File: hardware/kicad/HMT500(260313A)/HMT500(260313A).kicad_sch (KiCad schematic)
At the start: 0 parts

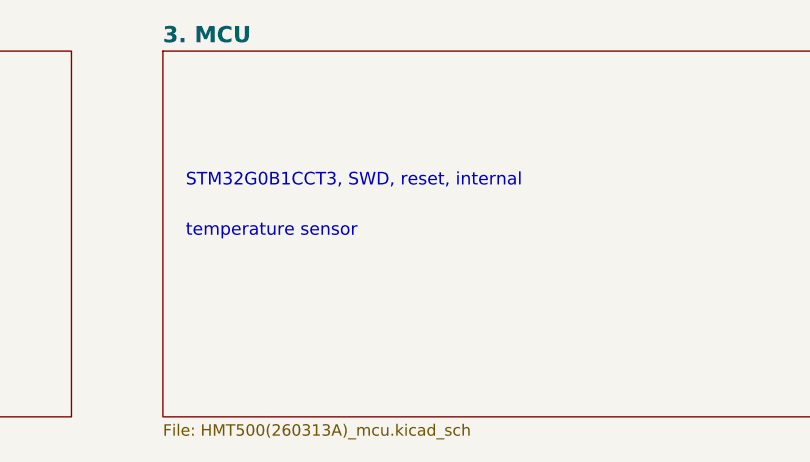
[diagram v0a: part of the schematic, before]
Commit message: Decision #39: sample stage uses JLCPCB parts - MCU STM32G0B1CCT6
Same die and pinout as CCT3 (85 C grade); revisit for production once the
electronics temperature spec is set. 58 of 60 BOM lines have LCSC numbers.

Co-Authored-By: Claude Opus 5.5 <noreply@anthropic.com>
Claude-Session: https://claude.ai/code/session_01JA2o8uJsqp9Vzsg4b665ev
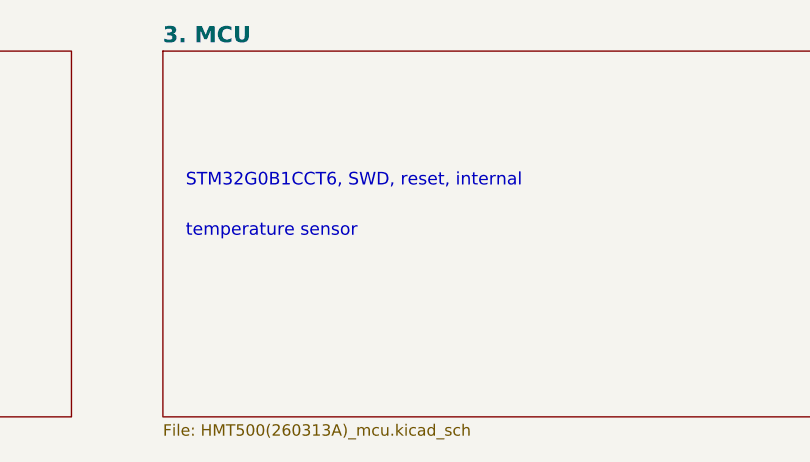
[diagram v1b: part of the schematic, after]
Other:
- note added: "STM32G0B1CCT6, SWD, reset, internal"
- note removed: "STM32G0B1CCT3, SWD, reset, internal"
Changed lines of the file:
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@@
 (text "LDO 3.3V" (at 119.38 56.388 0) (effects (font (size 1.4 1.4)) (justify left bottom)))
 (sheet (at 213.36 35.56) (size 86.36 40.64) (fields_autoplaced) (stroke (width 0.1524) (type solid)) (fill (color 0 0 0 0.0000)) (property "Sheetname" "3. MCU" (at 213.36 34.798 0) (effects (font (size 1.8 1.8) bold) (justify left bottom))) (property "Sheetfile" "HMT500(260313A)_mcu.kicad_sch" (at 213.36 76.962 0) (effects (font (size 1.27 1.27)) (justify left top))) (instances (project "HMT500(260313A)" (path "/1ebb025b-11bd-5f7c-aaab-41e2a750e8b3" (page "4")))))
-(text "STM32G0B1CCT3, SWD, reset, internal" (at 215.9 50.8 0) (effects (font (size 1.4 1.4)) (justify left bottom)))
+(text "STM32G0B1CCT6, SWD, reset, internal" (at 215.9 50.8 0) (effects (font (size 1.4 1.4)) (justify left bottom)))
 (text "temperature sensor" (at 215.9 56.388 0) (effects (font (size 1.4 1.4)) (justify left bottom)))
 (sheet (at 309.88 35.56) (size 86.36 40.64) (fields_autoplaced) (stroke (width 0.1524) (type solid)) (fill (color 0 0 0 0.0000)) (property "Sheetname" "4. Measurement" (at 309.88 34.798 0) (effects (font (size 1.8 1.8) bold) (justify left bottom))) (property "Sheetfile" "HMT500(260313A)_measurement.kicad_sch" (at 309.88 76.962 0) (effects (font (size 1.27 1.27)) (justify left top))) (instances (project "HMT500(260313A)" (path "/1ebb025b-11bd-5f7c-aaab-41e2a750e8b3" (page "5")))))
